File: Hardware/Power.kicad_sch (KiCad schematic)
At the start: 47 parts, among them U1 LT1963AEST-3.3#TRPBF, U2 TPS5405DR, U3 TPS2115ADRBR, U4 LT1963AEST-3.3#TRPBF

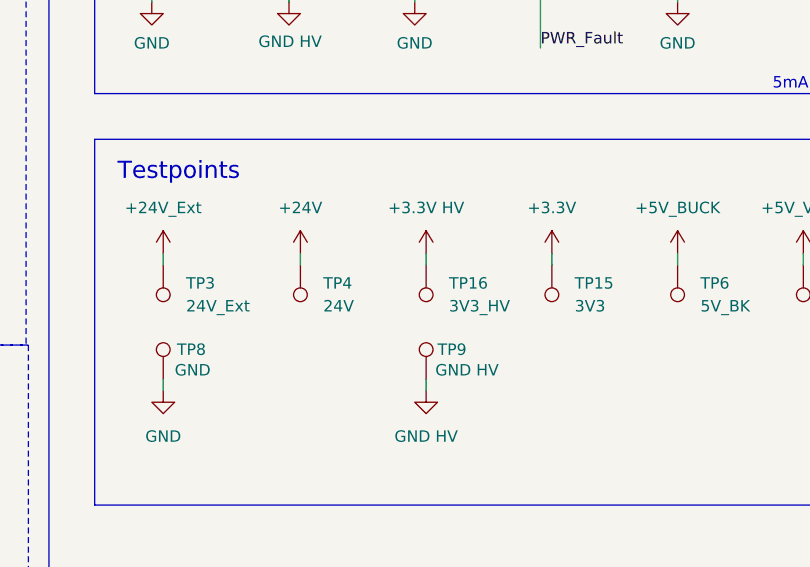
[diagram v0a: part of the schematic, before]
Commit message: added voltage reference, shunt model; addressed comments
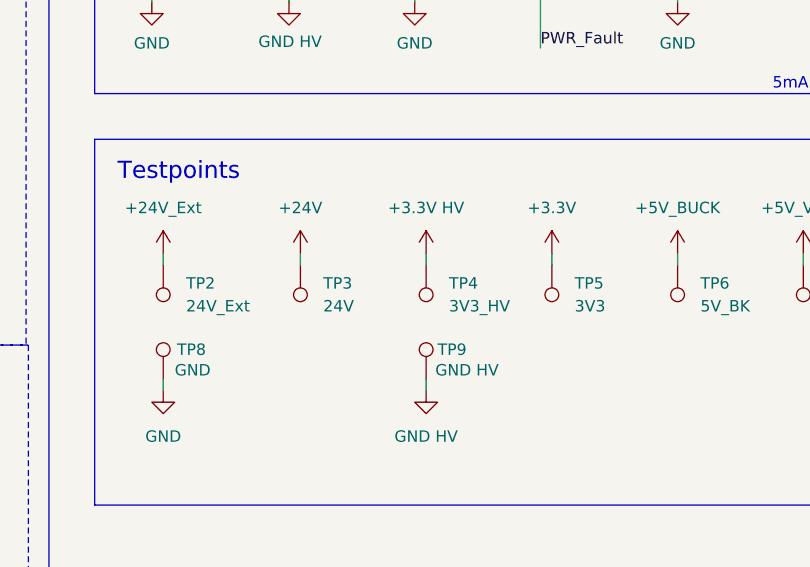
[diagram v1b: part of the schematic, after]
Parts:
- renumbered TP3 to TP2, TP4 to TP3, TP16 to TP4, TP15 to TP5

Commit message: lay out lay out
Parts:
- C1, C2: footprint Capacitor_SMD:C_0603_1608Metric_Pad1.08x0.95mm_HandSolder -> Capacitor_SMD:C_0805_2012Metric_Pad1.18x1.45mm_HandSolder; P/N (none) -> 08055D475KAT4A
- C17, C18, C3, C4, C5: footprint Capacitor_SMD:C_0603_1608Metric_Pad1.08x0.95mm_HandSolder -> Capacitor_SMD:C_0805_2012Metric_Pad1.18x1.45mm_HandSolder; P/N (none) -> GRM21BR61H106KE43K
- TP8, TP9: footprint (none) -> TestPoint:TestPoint_Pad_1.0x1.0mm
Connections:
- net +5V: now also C17.1, U4.1 (IN)
- net +5V_BUCK: no longer C17.1, U4.1 (IN)

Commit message: more routing
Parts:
- added TP15: GND, TestPoint:TestPoint_Pad_1.0x1.0mm, symbol Connector:TestPoint
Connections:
- net GND: now also TP15.1
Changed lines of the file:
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@@
 	(wire
 		(pts
+			(xy 199.39 138.43) (xy 199.39 139.7)
+		)
+		(stroke
+			(width 0)
+			(type default)
+		)
+	)
+	(wire
+		(pts
 			(xy 130.81 35.56) (xy 130.81 39.37)
 		)
@@
 	)
 	(symbol
+		(lib_id "Connector:TestPoint")
+		(at 199.39 138.43 0)
+		(mirror y)
+		(unit 1)
+		(exclude_from_sim no)
+		(in_bom yes)
+		(on_board yes)
+		(dnp no)
+		(property "Reference" "TP15"
+			(at 200.914 135.128 0)
+			(effects
+				(font
+					(size 1.27 1.27)
+				)
+				(justify right)
+			)
+		)
+		(property "Value" "GND"
+			(at 200.66 137.4141 0)
+			(effects
+				(font
+					(size 1.27 1.27)
+				)
+				(justify right)
+			)
+		)
+		(property "Footprint" "TestPoint:TestPoint_Pad_1.0x1.0mm"
+			(at 194.31 138.43 0)
+			(effects
+				(font
+					(size 1.27 1.27)
+				)
+				(hide yes)
+			)
+		)
+		(property "Datasheet" "~"
+			(at 194.31 138.43 0)
+			(effects
+				(font
+					(size 1.27 1.27)
+				)
+				(hide yes)
+			)
+		)
+		(property "Description" "test point"
+			(at 199.39 138.43 0)
+			(effects
+				(font
+					(size 1.27 1.27)
+				)
+				(hide yes)
+			)
+		)
+		(pin "1"
+		)
+		(instances
+			(project "PS-AmperesPCB"
+				(path "/a452d214-ea00-440d-a445-5d6103fda43a/3b2a70f8-48f8-45b9-b0fe-085893d574c0"
+					(reference "TP15")
+					(unit 1)
+				)
+			)
+		)
+	)
+	(symbol
 		(lib_id "power:+3.3V")
 		(at 215.9 77.47 0)
@@
 					(unit 1)
 				)
+			)
+		)
+	)
+	(symbol
+		(lib_id "power:GND")
+		(at 199.39 139.7 0)
+		(unit 1)
+		(exclude_from_sim no)
+		(in_bom yes)
+		(on_board yes)
+		(dnp no)
+		(fields_autoplaced yes)
+		(property "Reference" "#PWR040"
+			(at 199.39 146.05 0)
+			(effects
+				(font
+					(size 1.27 1.27)
+				)
+				(hide yes)
+			)
+		)
+		(property "Value" "GND"
+			(at 199.39 144.78 0)
+			(effects
+				(font
+					(size 1.27 1.27)
+				)
+			)
+		)
+		(property "Footprint" ""
+			(at 199.39 139.7 0)
+			(effects
+				(font
+					(size 1.27 1.27)
+				)
+				(hide yes)
+			)
+		)
+		(property "Datasheet" ""
+			(at 199.39 139.7 0)
+			(effects
+				(font
+					(size 1.27 1.27)
+				)
+				(hide yes)
+			)
+		)
+		(property "Description" "Power symbol creates a global label with name \"GND\" , ground"
+			(at 199.39 139.7 0)
+			(effects
+				(font
+					(size 1.27 1.27)
+				)
+				(hide yes)
+			)
+		)
+		(pin "1"
+		)
+		(instances
+			(project "PS-AmperesPCB"
+				(path "/a452d214-ea00-440d-a445-5d6103fda43a/3b2a70f8-48f8-45b9-b0fe-085893d574c0"
+					(reference "#PWR040")
+					(unit 1)
+				)

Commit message: updated some component part nums
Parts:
- C1, C2: Mfg (none) -> 08055D475KAT4A
- C10, C11, C17, C18, C3, C4, C5, C7, C9: Mfg (none) -> GRM21BR61H106KE43K
- C12: Mfg (none) -> CL10B103KB8NNNC; P/N MSASH168SB5103KTNA01 -> CL10B103KB8NNNC
- C13: Mfg (none) -> 06035C332K4T2A
- C14, C15, C6: Mfg (none) -> MLASH168SB7104KTNA01
- C16, C8: Mfg (none) -> MLASU168SB5105KTNA01
- R1: Mfg SDR10EZPJ152 -> CRCW06034K30FKEA; P/N (none) -> CRCW06034K30FKEA
- R2, R3: Mfg SDR10EZPJ152 -> CRCW0603120RFKEC; P/N (none) -> CRCW0603120RFKEC
- R4: Mfg (none) -> CRCW06034K30FKEA; P/N CRCW06034K30FKTA -> CRCW06034K30FKEA
- R5: Mfg (none) -> CRCW0603768RFKEA
- R6: Mfg (none) -> CRCW060316K0FKTA
- R8: Mfg (none) -> CRCW060310K0FKEI
- R9: Mfg (none) -> CRCW0603332RFKEAHP

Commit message: generated production stuff
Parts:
- D1, D2, D3: P/N (none) -> XL-1608UBC-06A
- D4: Mfg (none) -> NCD0603R1
- D5: Mfg (none) -> XL-1608UBC-06A
- D6: Mfg (none) -> SS24FL
- PS1: P/N (none) -> 1769205341
- U1, U4: P/N (none) -> LT1963AEST-3.3#TRPBF
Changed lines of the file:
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@@
 			)
 		)
+		(property "Mfg" "SS24FL"
+			(at 101.6 101.6 90)
+			(effects
+				(font
+					(size 1.27 1.27)
+				)
+				(hide yes)
+			)
+		)
 		(pin "2"
 		)
@@
 			)
 		)
+		(property "Mfg" "XL-1608UBC-06A"
+			(at 245.11 91.44 90)
+			(effects
+				(font
+					(size 1.27 1.27)
+				)
+				(hide yes)
+			)
+		)
 		(pin "2"
 		)
@@
 			)
 		)
+		(property "P/N" "LT1963AEST-3.3#TRPBF"
+			(at 146.05 160.02 0)
+			(effects
+				(font
+					(size 1.27 1.27)
+				)
+				(hide yes)
+			)
+		)
 		(pin "3"
 		)
@@
 			)
 		)
+		(property "P/N" "XL-1608UBC-06A"
+			(at 215.9 91.44 90)
+			(effects
+				(font
+					(size 1.27 1.27)
+				)
+				(hide yes)
+			)
+		)
 		(pin "1"
 		)
@@
 			)
 		)
+		(property "P/N" "XL-1608UBC-06A"
+			(at 201.93 91.44 90)
+			(effects
+				(font
+					(size 1.27 1.27)
+				)
+				(hide yes)
+			)
+		)
 		(pin "1"
 		)
@@
 			)
 		)
+		(property "P/N" "LT1963AEST-3.3#TRPBF"
+			(at 114.3 41.91 0)
+			(effects
+				(font
+					(size 1.27 1.27)
+				)
+				(hide yes)
+			)
+		)
 		(pin "3"
 		)
@@
 			)
 		)
+		(property "P/N" "1769205341"
+			(at 41.91 39.37 0)
+			(effects
+				(font
+					(size 1.27 1.27)
+				)
+				(hide yes)
+			)
+		)
 		(pin "8"
 		)
@@
 			)
 		)
+		(property "P/N" "XL-1608UBC-06A"
+			(at 186.69 91.44 90)
+			(effects
+				(font
+					(size 1.27 1.27)
+				)
+				(hide yes)
+			)
+		)
 		(pin "1"
 		)
@@
 			(at 229.87 91.44 90)
 			(effects
+				(font
+					(size 1.27 1.27)
+				)
+				(hide yes)
+			)
+		)
+		(property "Mfg" "NCD0603R1"
+			(at 229.87 91.44 90)
+			(effects
